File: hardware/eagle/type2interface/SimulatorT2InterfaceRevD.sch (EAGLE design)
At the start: 25 parts, among them IC1 7805T, IC2 MAX233, IC3 ATMEGA328P_PDIP

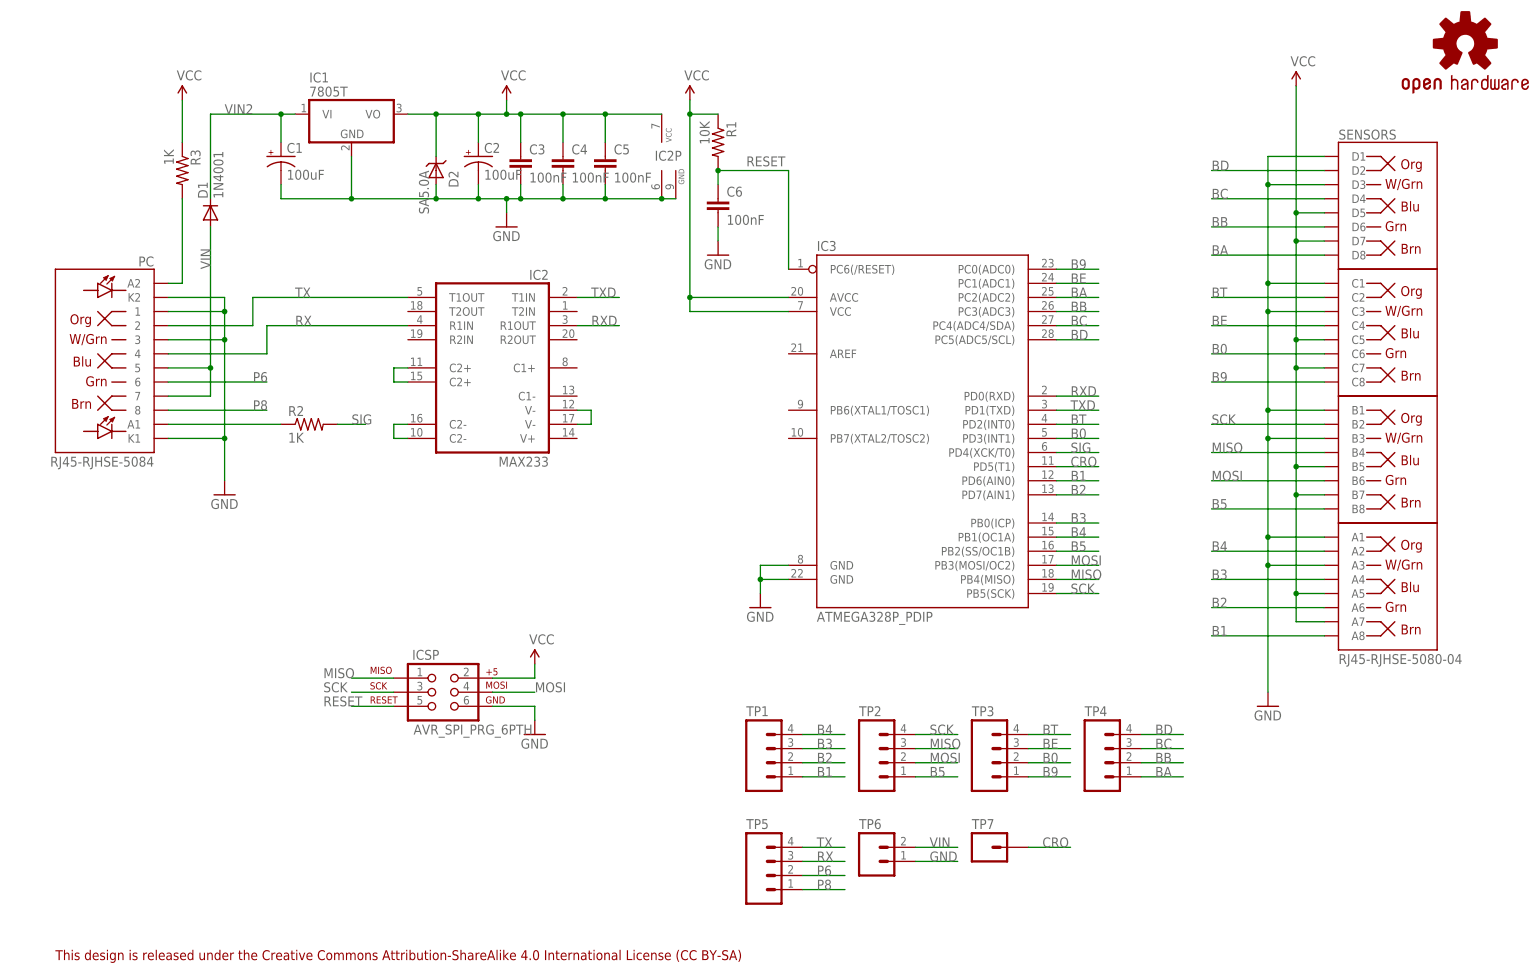
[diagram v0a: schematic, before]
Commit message: Interface Board Rev D
Fixes a clearance problem with the alternative voltage regulator, and
adds a second serial connection for future use. Enable layer 51 tDocu in
Eagle to see alternate regulator outline. Closes #1
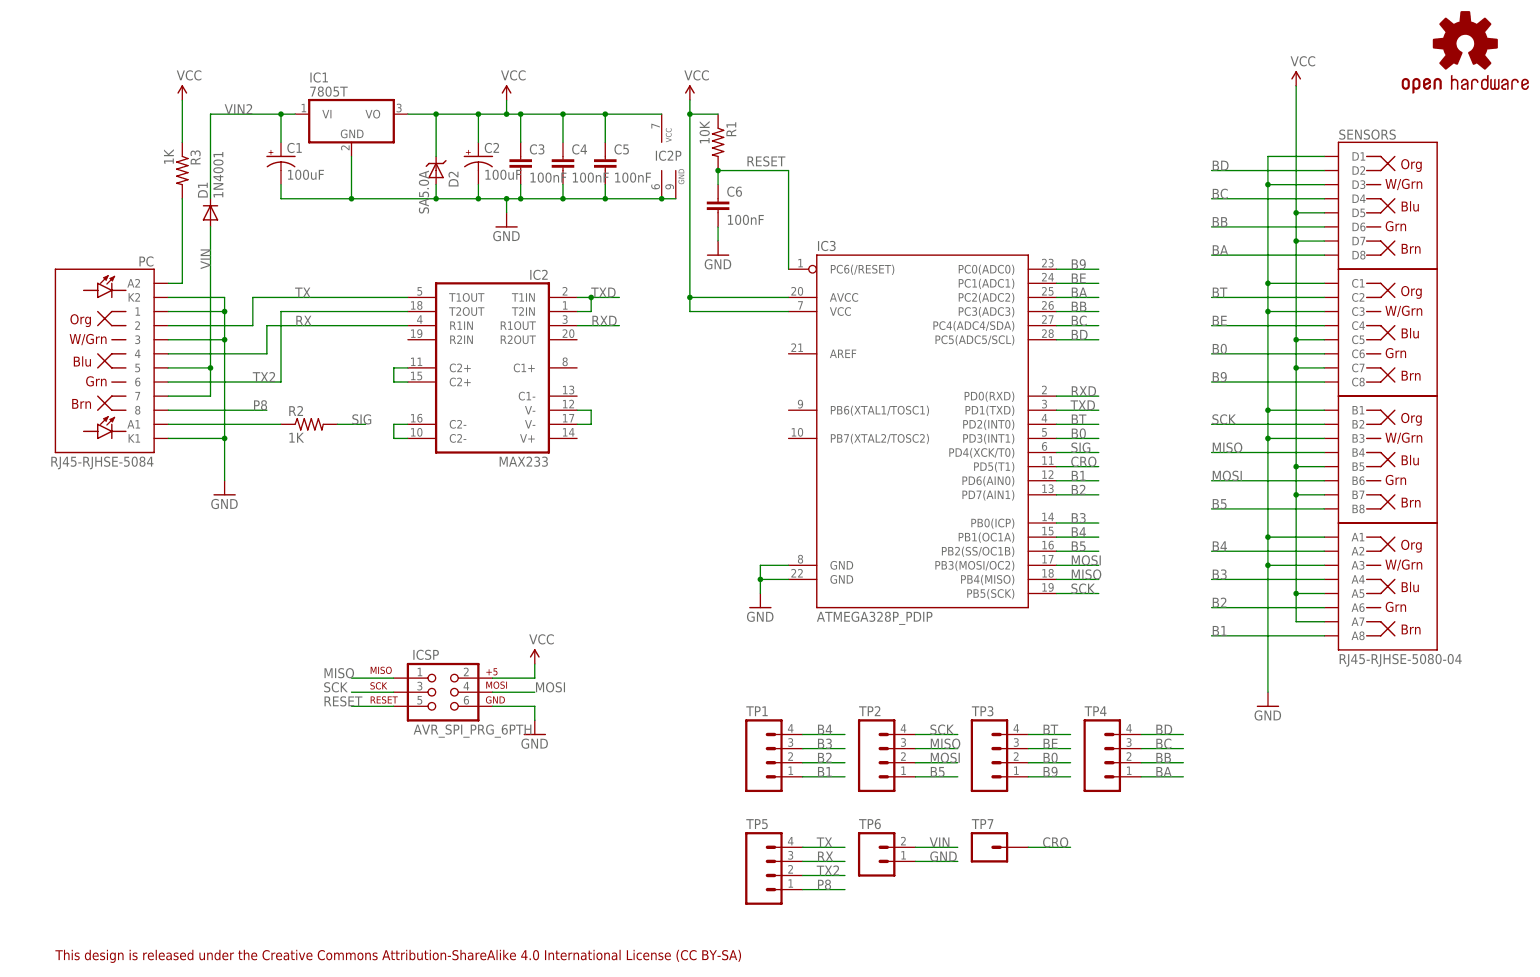
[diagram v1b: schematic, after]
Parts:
- IC1: device linear:7805T -> AIC_Custom:7805T
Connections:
- removed net P6: PC.6, TP5.2
- new net TX2: IC2G$1.T2OUT, PC.6, TP5.2
- net TXD: now also IC2G$1.T2IN
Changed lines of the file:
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@@
 <part name="FRAME1" library="SparkFun-Aesthetics" deviceset="FRAME-A4L" device="">
 <attribute name="CNAME" value="Liverpool Simulator Type 2 Interface"/>
-<attribute name="CREVISION" value="Rev C 09/2018"/>
+<attribute name="CREVISION" value="Rev D 01/2019"/>
 <attribute name="DESIGNER" value="A J Instone-Cowie"/>
 </part>
@@
 <part name="C6" library="SparkFun-Capacitors" deviceset="CAP" device="PTH" value="100nF"/>
 <part name="GND18" library="SparkFun-Aesthetics" deviceset="GND" device=""/>
-<part name="IC1" library="linear" deviceset="78*" device="T" technology="05" value="7805T"/>
+<part name="IC1" library="AIC_Custom" deviceset="7805" device="T" value="7805T"/>
 <part name="LOGO1" library="SparkFun-Aesthetics" deviceset="OSHW-LOGO" device="S"/>
 <part name="D2" library="AIC_Custom" deviceset="SA5.0A" device=""/>
@@
 <segment>
 <pinref part="IC2" gate="G$1" pin="T1IN"/>
-<wire x1="104.14" y1="132.08" x2="111.76" y2="132.08" width="0.1524" layer="91"/>
+<wire x1="104.14" y1="132.08" x2="106.68" y2="132.08" width="0.1524" layer="91"/>
 <label x="106.68" y="132.08" size="1.778" layer="95"/>
+<pinref part="IC2" gate="G$1" pin="T2IN"/>
+<wire x1="106.68" y1="132.08" x2="111.76" y2="132.08" width="0.1524" layer="91"/>
+<wire x1="104.14" y1="129.54" x2="106.68" y2="129.54" width="0.1524" layer="91"/>
+<wire x1="106.68" y1="129.54" x2="106.68" y2="132.08" width="0.1524" layer="91"/>
+<junction x="106.68" y="132.08"/>
 </segment>
 </net>
@@
 </segment>
 </net>
-<net name="P6" class="0">
-<segment>
-<pinref part="TP5" gate="G$1" pin="2"/>
-<wire x1="144.78" y1="27.94" x2="152.4" y2="27.94" width="0.1524" layer="91"/>
-<label x="147.32" y="27.94" size="1.778" layer="95"/>
-</segment>
-<segment>
-<pinref part="PC" gate="G$1" pin="6"/>
-<wire x1="30.48" y1="116.84" x2="48.26" y2="116.84" width="0.1524" layer="91"/>
-<label x="45.72" y="116.84" size="1.778" layer="95"/>
-</segment>
-</net>
 <net name="P8" class="0">
 <segment>
@@
 </segment>
 </net>
+<net name="TX2" class="0">
+<segment>
+<pinref part="IC2" gate="G$1" pin="T2OUT"/>
+<wire x1="73.66" y1="129.54" x2="50.8" y2="129.54" width="0.1524" layer="91"/>
+<wire x1="50.8" y1="129.54" x2="50.8" y2="116.84" width="0.1524" layer="91"/>
+<pinref part="PC" gate="G$1" pin="6"/>
+<wire x1="50.8" y1="116.84" x2="30.48" y2="116.84" width="0.1524" layer="91"/>
+<label x="45.72" y="116.84" size="1.778" layer="95"/>
+</segment>
+<segment>
+<pinref part="TP5" gate="G$1" pin="2"/>
+<wire x1="144.78" y1="27.94" x2="152.4" y2="27.94" width="0.1524" layer="91"/>
+<label x="147.32" y="27.94" size="1.778" layer="95"/>
+</segment>
+</net>
